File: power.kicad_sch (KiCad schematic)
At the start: 0 parts

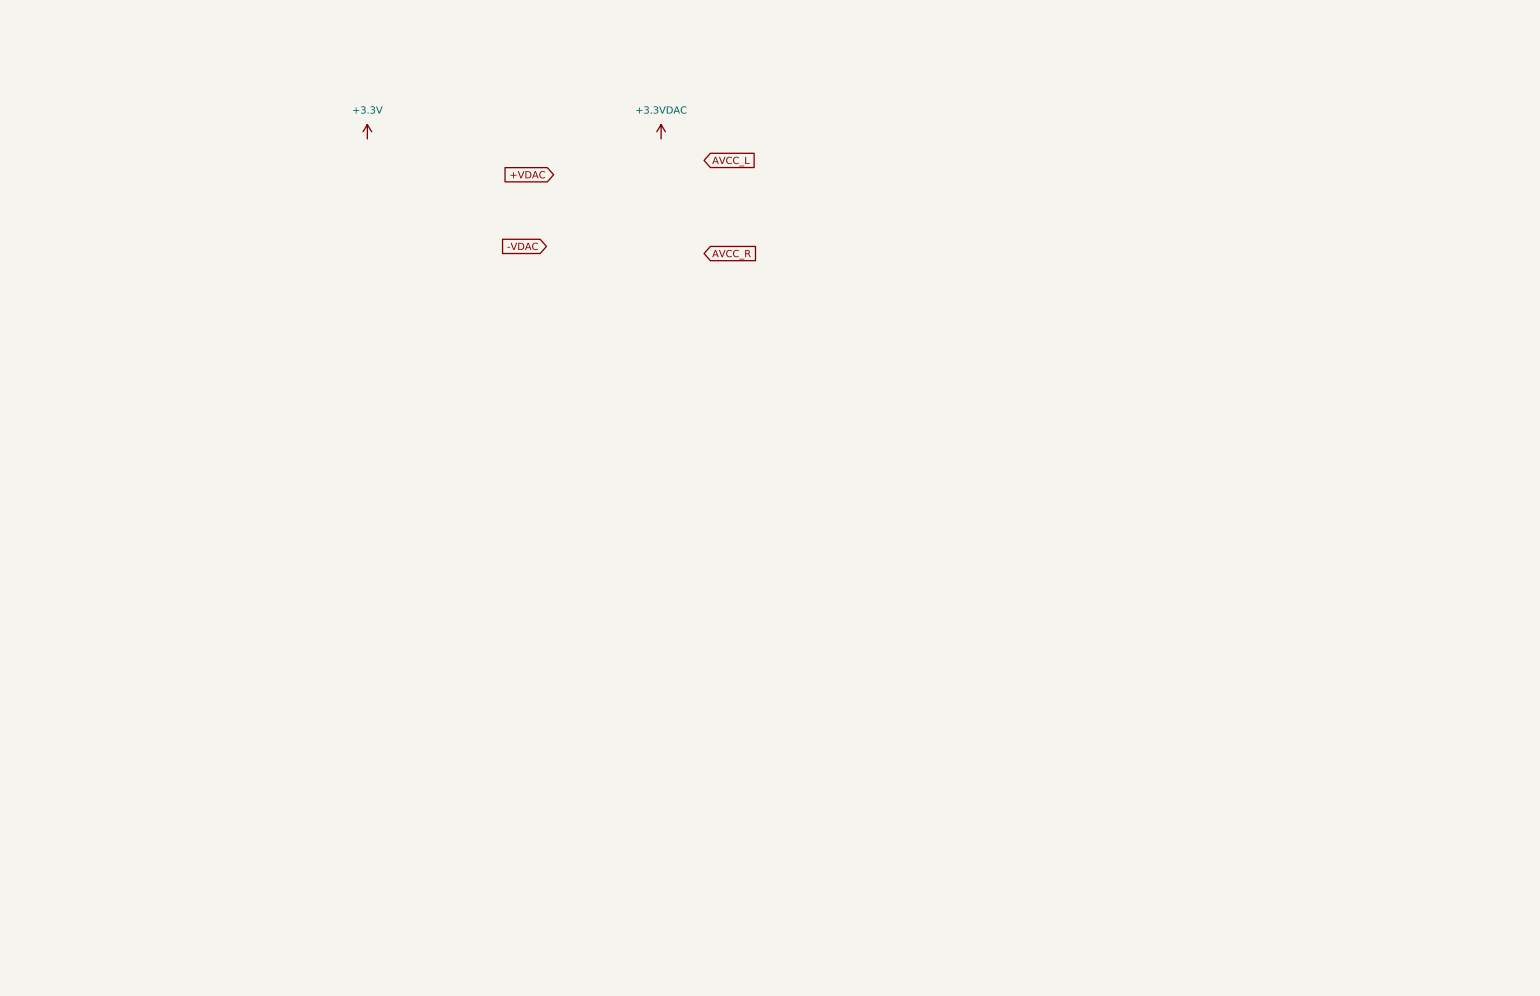
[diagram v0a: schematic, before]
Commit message: Adding values to output stage
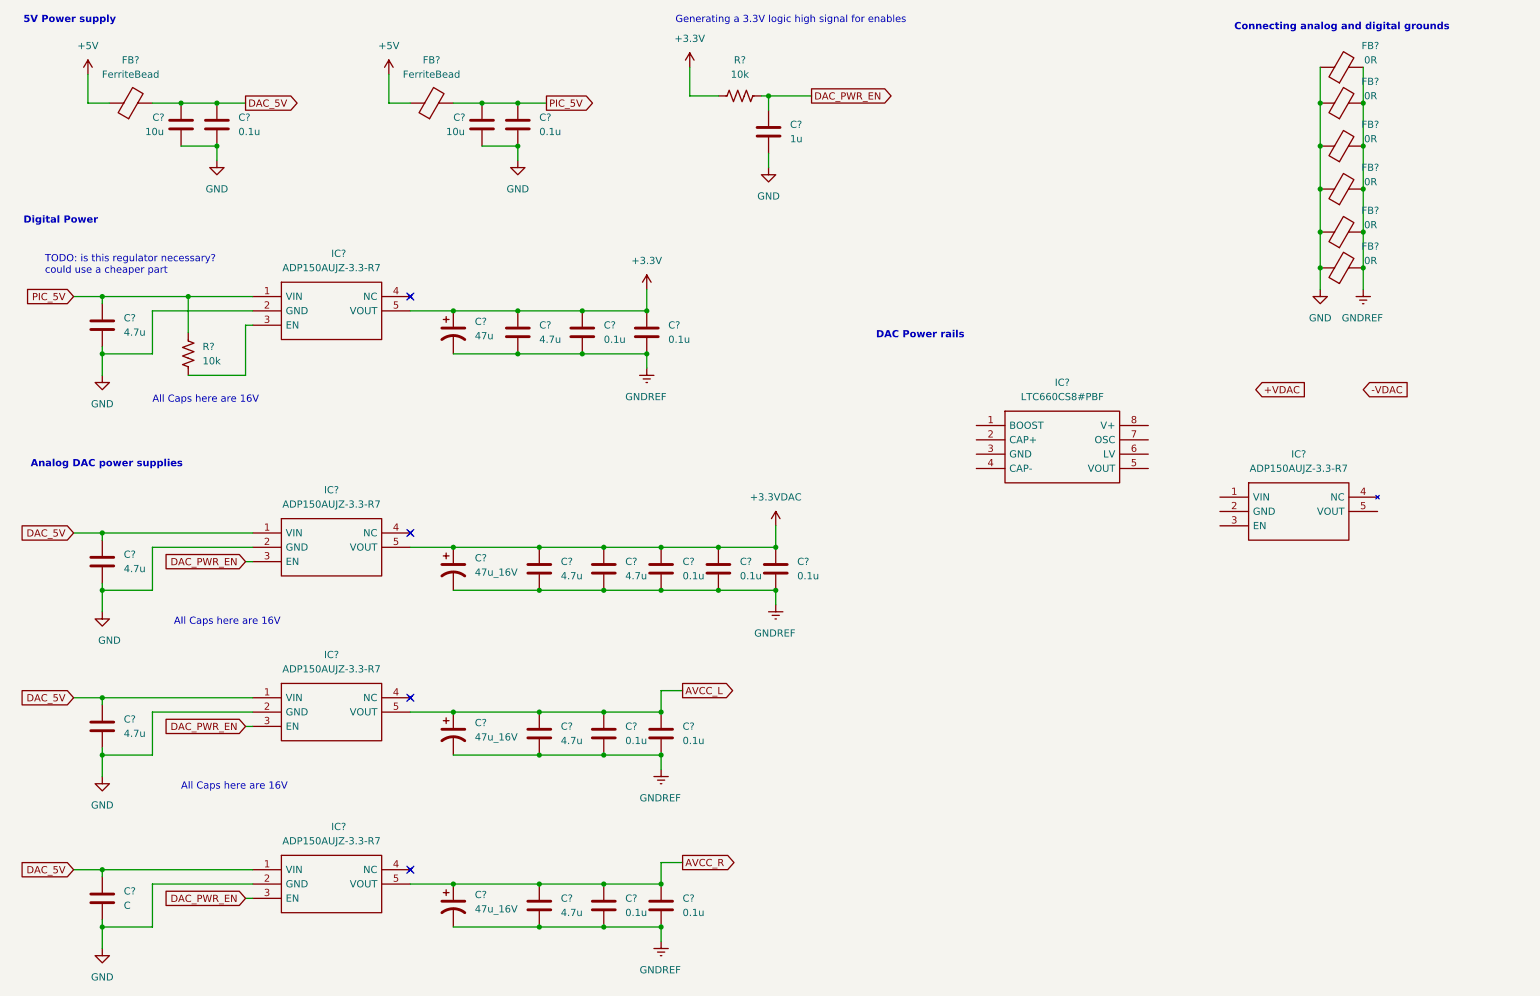
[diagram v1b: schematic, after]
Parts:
- added C? (x11): 0.1u, symbol Device:C
- added C? (x8): 4.7u, symbol Device:C
- added C? (x3): 47u_16V, symbol Device:C_Polarized_US
- added C?: 47u, symbol Device:C_Polarized_US
- added C?: C, symbol Device:C
- added C? (x2): 10u, symbol Device:C
- added C?: 1u, symbol Device:C
- added FB? (x6): 0R, symbol Device:FerriteBead
- added FB? (x2): FerriteBead, symbol Device:FerriteBead
- added IC? (x5): ADP150AUJZ-3.3-R7, SOT95P280X100-5N, symbol SamacSys_Parts:ADP150AUJZ-3.3-R7
- added IC?: LTC660CS8#PBF, SOIC127P599X175-8N, symbol SamacSys_Parts:LTC660CS8#PBF
- added R? (x2): 10k, symbol Device:R_US
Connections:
- net +3.3VDAC: now also C?.1, C?.1, C?.1, C?.1, C?.1, C?.1, IC?.5 (VOUT)
- net +3V3: now also C?.1, C?.1, C?.1, C?.1, IC?.5 (VOUT), R?.1
- net AVCC_L: now also C?.1, C?.1, C?.1, C?.1, IC?.5 (VOUT)
- net AVCC_R: now also C?.1, C?.1, C?.1, C?.1, IC?.5 (VOUT)
- new net: IC?.3 (EN), R?.1
- new net +5V: FB?.1, FB?.1
- new net DAC_5V: C?.1, C?.1, C?.1, C?.1, C?.2, FB?.2, IC?.1 (VIN), IC?.1 (VIN), IC?.1 (VIN)
- new net DAC_PWR_EN: C?.1, IC?.3 (EN), IC?.3 (EN), IC?.3 (EN), R?.2
- new net GND: C?.1, C?.1, C?.2, C?.2, C?.2, C?.2, C?.2, C?.2, C?.2, FB?.1, FB?.1, FB?.1, FB?.1, FB?.1, FB?.1, IC?.2 (GND), IC?.2 (GND), IC?.2 (GND), IC?.2 (GND)
- new net GNDREF: C?.2, C?.2, C?.2, C?.2, C?.2, C?.2, C?.2, C?.2, C?.2, C?.2, C?.2, C?.2, C?.2, C?.2, C?.2, C?.2, C?.2, C?.2, FB?.2, FB?.2, FB?.2, FB?.2, FB?.2, FB?.2
- new net PIC_5V: C?.1, C?.1, C?.2, FB?.2, IC?.1 (VIN), R?.2
- no-connect marks 0 -> 4
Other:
- note added: "5V Power supply"
- note added: "All Caps here are 16V"
- note added: "Analog DAC power supplies"
- note added: "Connecting analog and digital grounds"
- note added: "DAC Power rails"
- note added: "Digital Power"
- note added: "Generating a 3.3V logic high signal for enables"
- note added: "TODO: is this regulator necessary? could use a cheaper part"
- title: (none) -> Power Supplies

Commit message: Redoing power stage and changing output stage accordingly
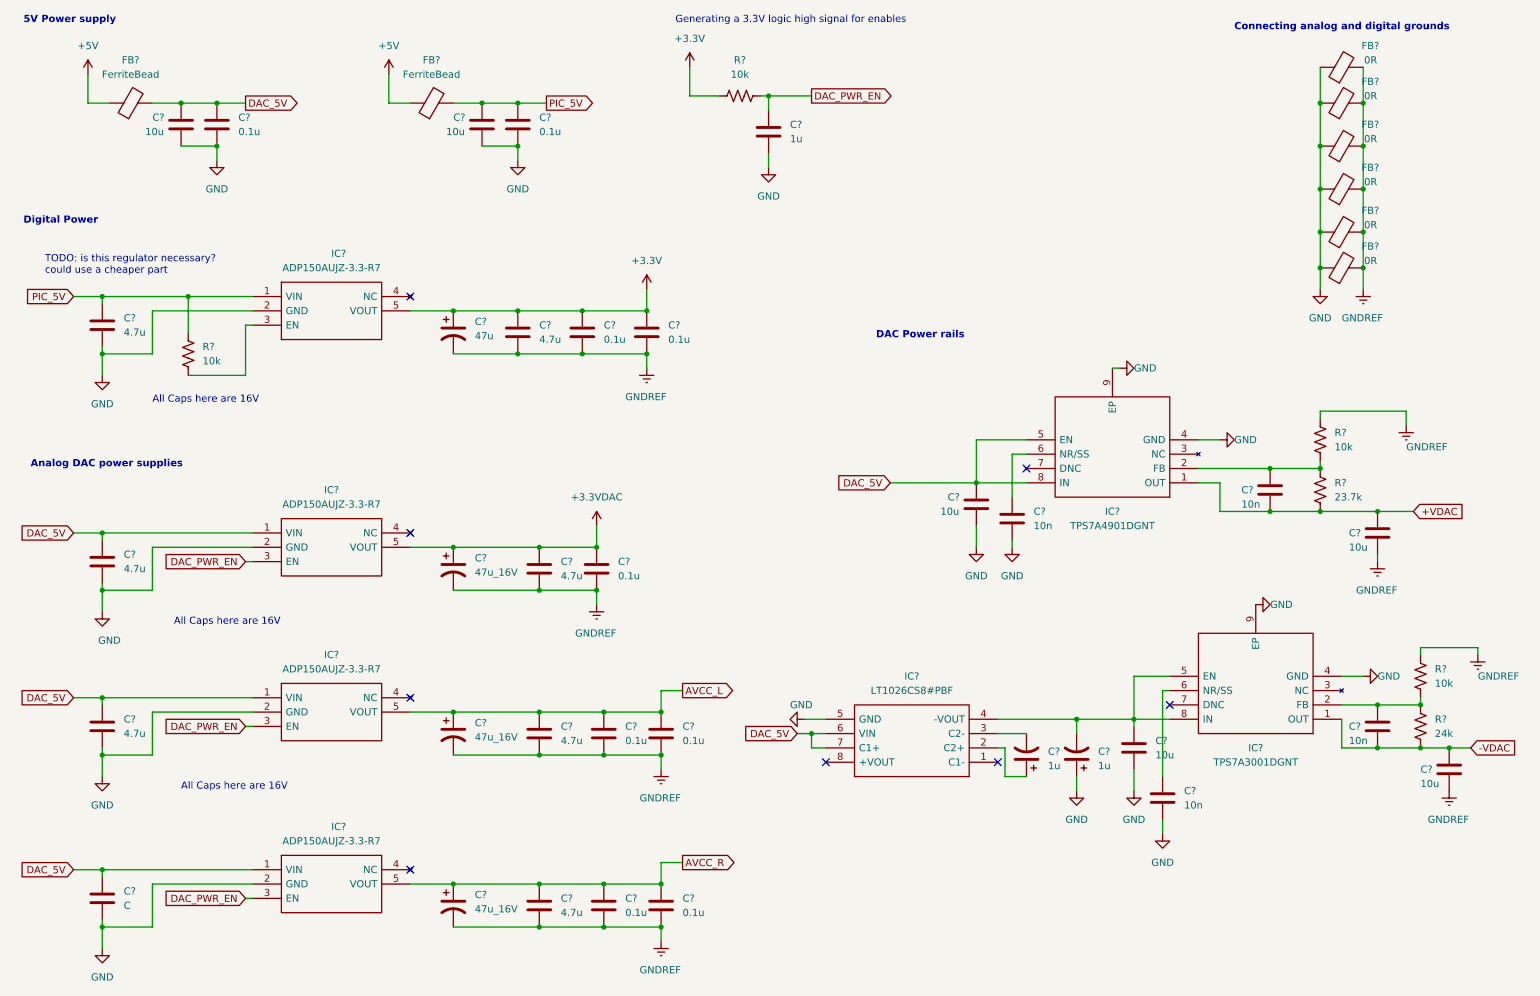
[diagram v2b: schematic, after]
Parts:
- removed C? (x2): 0.1u, symbol Device:C
- removed C?: 4.7u, symbol Device:C
- removed IC?: ADP150AUJZ-3.3-R7, SOT95P280X100-5N, symbol SamacSys_Parts:ADP150AUJZ-3.3-R7
- removed IC?: LTC660CS8#PBF, SOIC127P599X175-8N, symbol SamacSys_Parts:LTC660CS8#PBF
- added C? (x4): 10n, symbol Device:C
- added C? (x4): 10u, symbol Device:C
- added C? (x2): 1u, symbol Device:C_Polarized_US
- added IC?: LT1026CS8#PBF, SOIC127P599X175-8N, symbol SamacSys_Parts:LT1026CS8#PBF
- added IC?: TPS7A3001DGNT, SOP65P490X110-9N, symbol SamacSys_Parts:TPS7A3001DGNT
- added IC?: TPS7A4901DGNT, SOP65P490X110-9N, symbol SamacSys_Parts:TPS7A4901DGNT
- added R? (x2): 10k, symbol Device:R_US
- added R?: 24k, symbol Device:R_US
- added R?: 23.7k, symbol Device:R_US
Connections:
- net +VDAC: now also C?.1, C?.2, IC?.1 (OUT), R?.1
- net -VDAC: now also C?.1, C?.2, IC?.1 (OUT), R?.1
- net DAC_5V: now also C?.1, IC?.5 (EN), IC?.6 (VIN), IC?.7 (C1+), IC?.8 (IN)
- net GND: now also C?.1, C?.2, C?.2, C?.2, C?.2, IC?.4 (GND), IC?.4 (GND), IC?.5 (GND), IC?.9 (EP), IC?.9 (EP)
- net GNDREF: now also C?.2, C?.2, R?.2, R?.2
- new net: C?.1, IC?.2 (C2+)
- new net: C?.2, IC?.3 (C2-)
- new net: C?.1, C?.2, IC?.4 (-VOUT), IC?.5 (EN), IC?.8 (IN)
- new net: C?.1, IC?.2 (FB), R?.1, R?.2 (x2)
- new net: C?.1, IC?.6 (NR/SS) (x2)
- no-connect marks 4 -> 8
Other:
- moved on the sheet: C?
